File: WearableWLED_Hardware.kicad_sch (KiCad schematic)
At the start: 20 parts, among them J1 LED_OUT, P1 USB_C_Receptacle_USB2.0_14P, SW1 SWITCH, SW2 SW_SPDT, U1 ESP32-C3-MINI-1, U2 MCP73811T-420I-OT

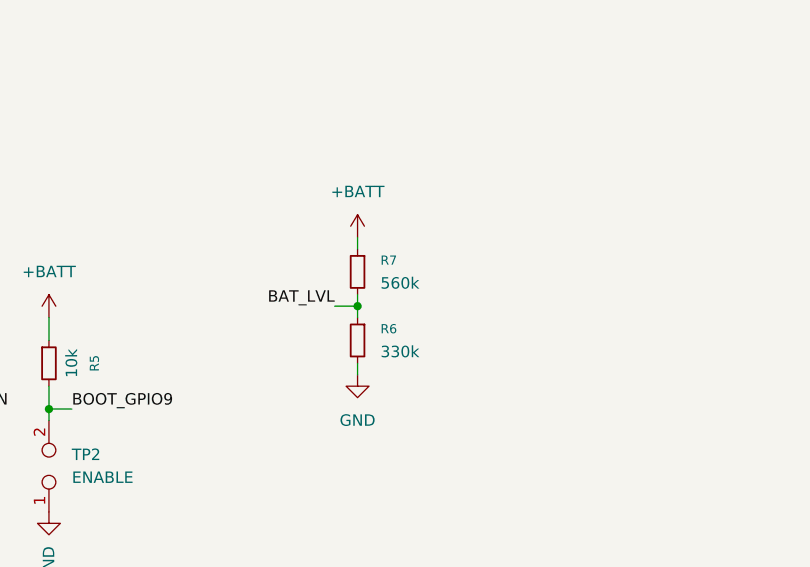
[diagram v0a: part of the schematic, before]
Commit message: Change voltage divider value for battery
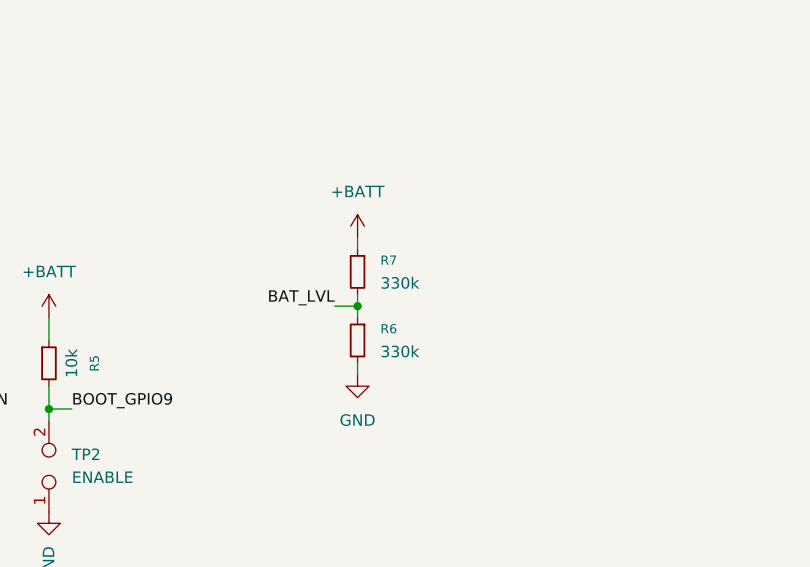
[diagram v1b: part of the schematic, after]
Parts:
- R7: value 560k -> 330k
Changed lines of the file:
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@@
 			)
 		)
-		(property "Value" "560k"
+		(property "Value" "330k"
 			(at 189.23 128.2699 0)
 			(effects
